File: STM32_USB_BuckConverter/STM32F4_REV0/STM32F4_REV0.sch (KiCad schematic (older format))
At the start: 44 parts

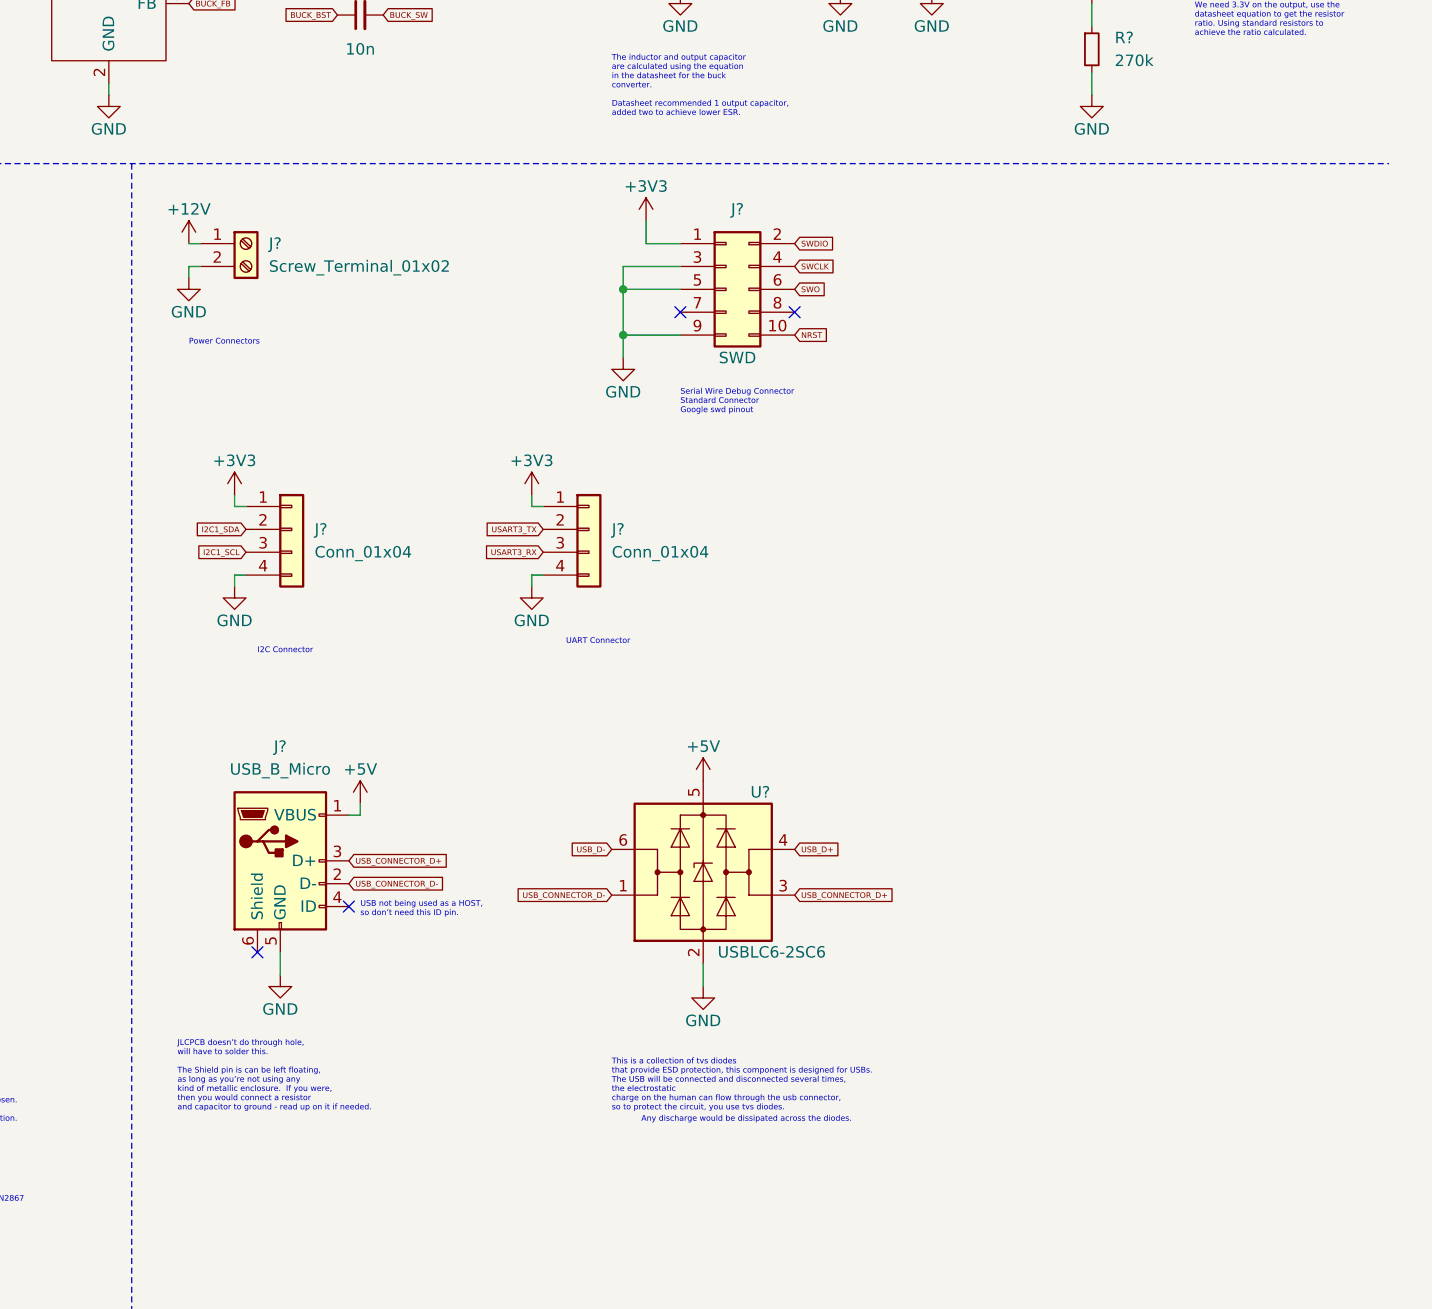
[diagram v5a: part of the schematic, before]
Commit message: rearranged schematic to make it readable.
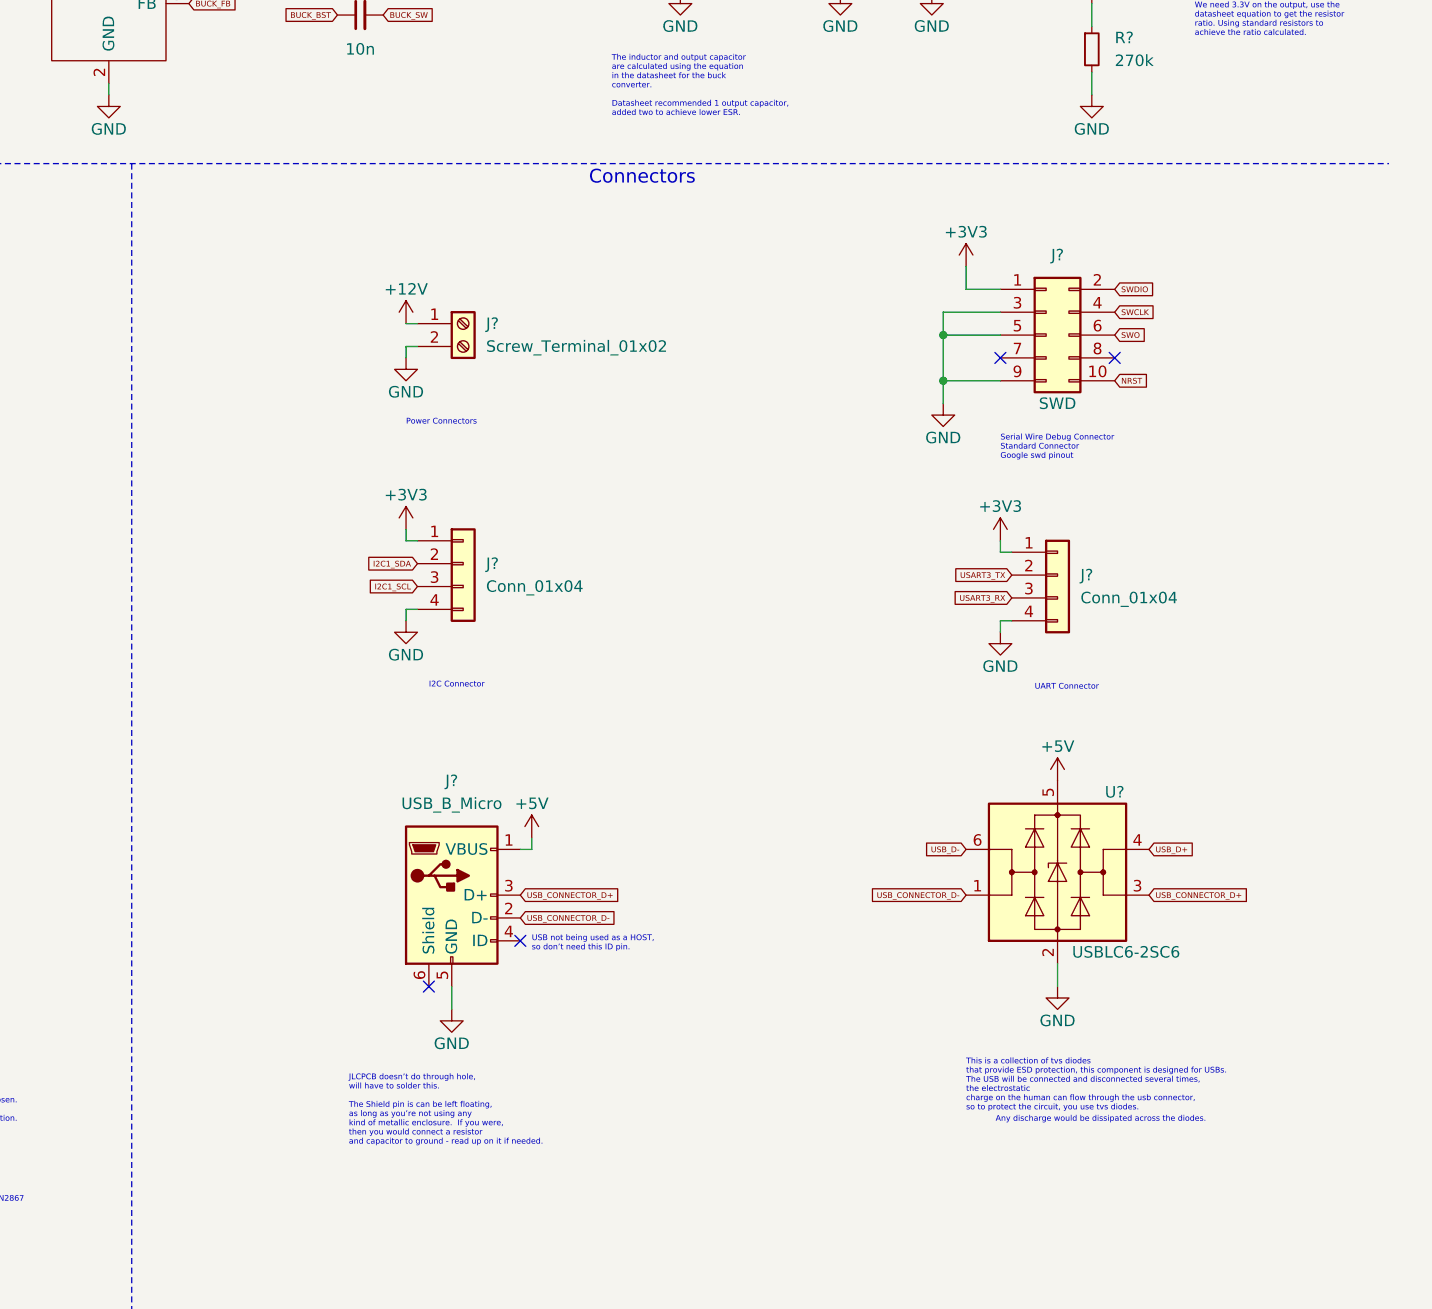
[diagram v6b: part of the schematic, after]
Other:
- note added: "Connectors"
- moved on the sheet: J?, U?

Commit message: Performed ERC, ignorable warnings rejects.
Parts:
- added D3: RED, symbol Device:LED_Small
- added R6: 1k, symbol Device:R_Small
- R5: renamed from R?; value 270k -> 270
- gave numbers to parts that had none: 43
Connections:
- net +3V3: now also D3.2 (A)
- net GND: now also R6.1
- new net: D3.1 (K), R6.2
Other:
- note added: "Connectors and USB"
- note removed: "Connectors"
- moved on the sheet: C3, C4, D2, L1, R3, R4, R5

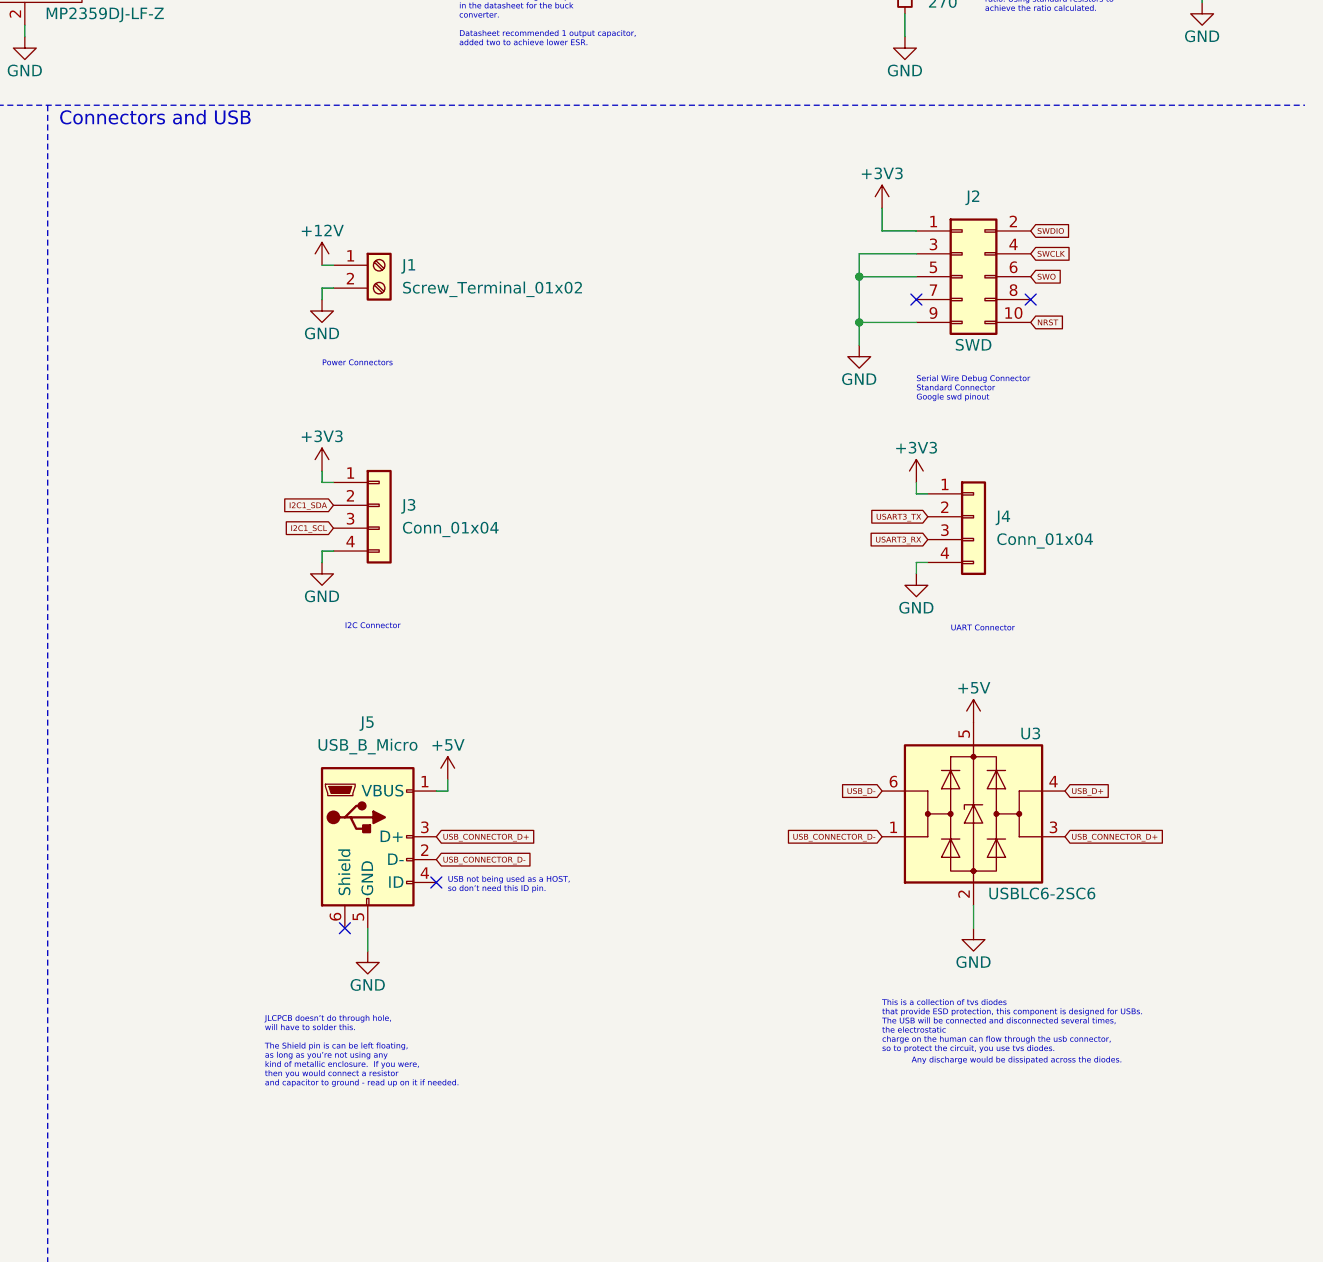
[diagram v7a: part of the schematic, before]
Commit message: Added footprints for all the schematic symbols.
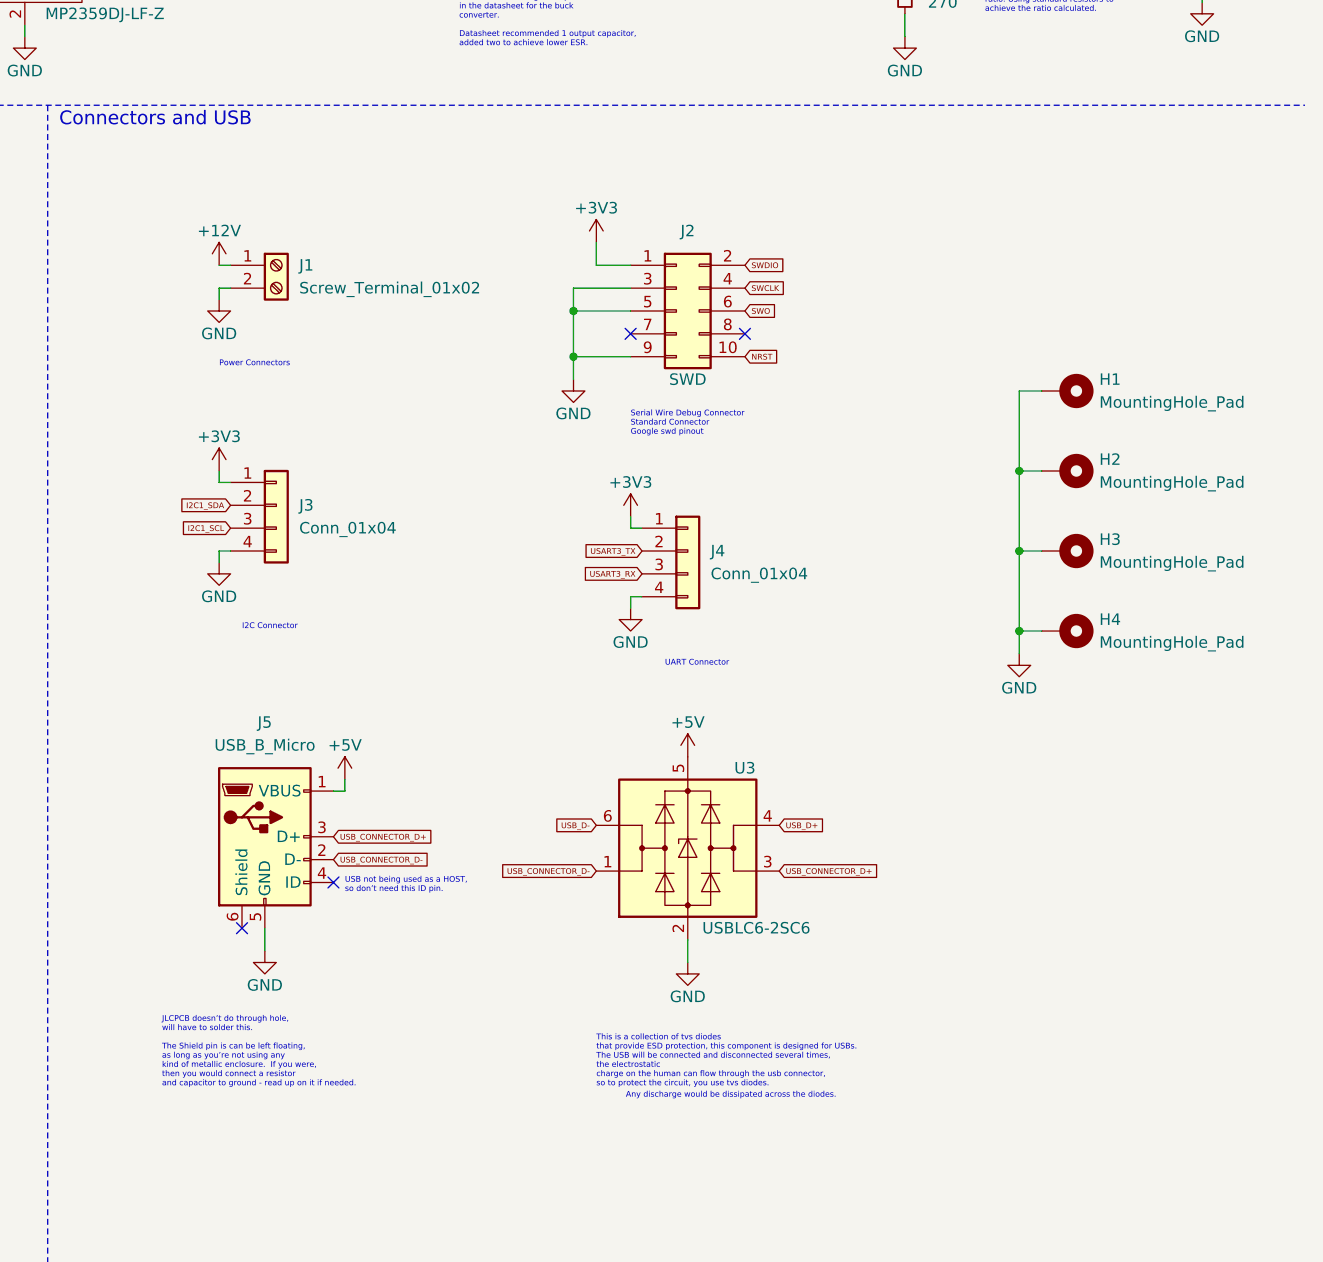
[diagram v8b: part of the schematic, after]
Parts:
- added H1, H2, H3, H4: MountingHole_Pad, MountingHole:MountingHole_4.3mm_M4_Pad_Via, symbol Mechanical:MountingHole_Pad
- C1, C3, C4: footprint (none) -> Capacitor_SMD:C_1206_3216Metric
- C10, C11, C12, C15, C16, C6, C7, C8, C9: footprint (none) -> Capacitor_SMD:C_0402_1005Metric
- C13, C14, C2, C5: footprint (none) -> Capacitor_SMD:C_0603_1608Metric
- D1, D2: footprint (none) -> Diode_SMD:D_SOD-123
- D3, D4: footprint (none) -> LED_SMD:LED_0603_1608Metric
- F1: footprint (none) -> Fuse:Fuse_1206_3216Metric
- FB1: footprint (none) -> Inductor_SMD:L_0805_2012Metric
- J1: footprint (none) -> TerminalBlock_Phoenix:TerminalBlock_Phoenix_PT-1,5-2-3.5-H_1x02_P3.50mm_Horizontal
- J2: footprint (none) -> Connector_PinHeader_1.27mm:PinHeader_2x05_P1.27mm_Vertical_SMD
- J3, J4: footprint (none) -> Connector_Molex:Molex_PicoBlade_53048-0410_1x04_P1.25mm_Horizontal
- J5: footprint (none) -> Connector_USB:USB_Micro-B_Molex-105017-0001
- L1: footprint (none) -> Inductor_SMD:L_Sunlord_MWSA0518_5.4x5.2mm
- L2: footprint (none) -> Inductor_SMD:L_0402_1005Metric
- R1, R2, R3, R4, R5, R6, R9: footprint (none) -> Resistor_SMD:R_0603_1608Metric
- R10, R11, R7, R8: footprint (none) -> Resistor_SMD:R_0402_1005Metric
- SW1: footprint (none) -> Button_Switch_SMD:SW_SPDT_PCM12
- U1: footprint (none) -> Package_TO_SOT_SMD:SOT-23-6
- Y1: footprint (none) -> Crystal:Crystal_SMD_3225-4Pin_3.2x2.5mm
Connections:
- net GND: now also H1.1, H2.1, H3.1, H4.1
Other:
- moved on the sheet: J1, J2, J3, J4, J5, U3
